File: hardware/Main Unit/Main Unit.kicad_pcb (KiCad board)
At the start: 2 copper layers, 6 parts, among them U1 MCXN547VKLT, U2 TLV71333PDBV

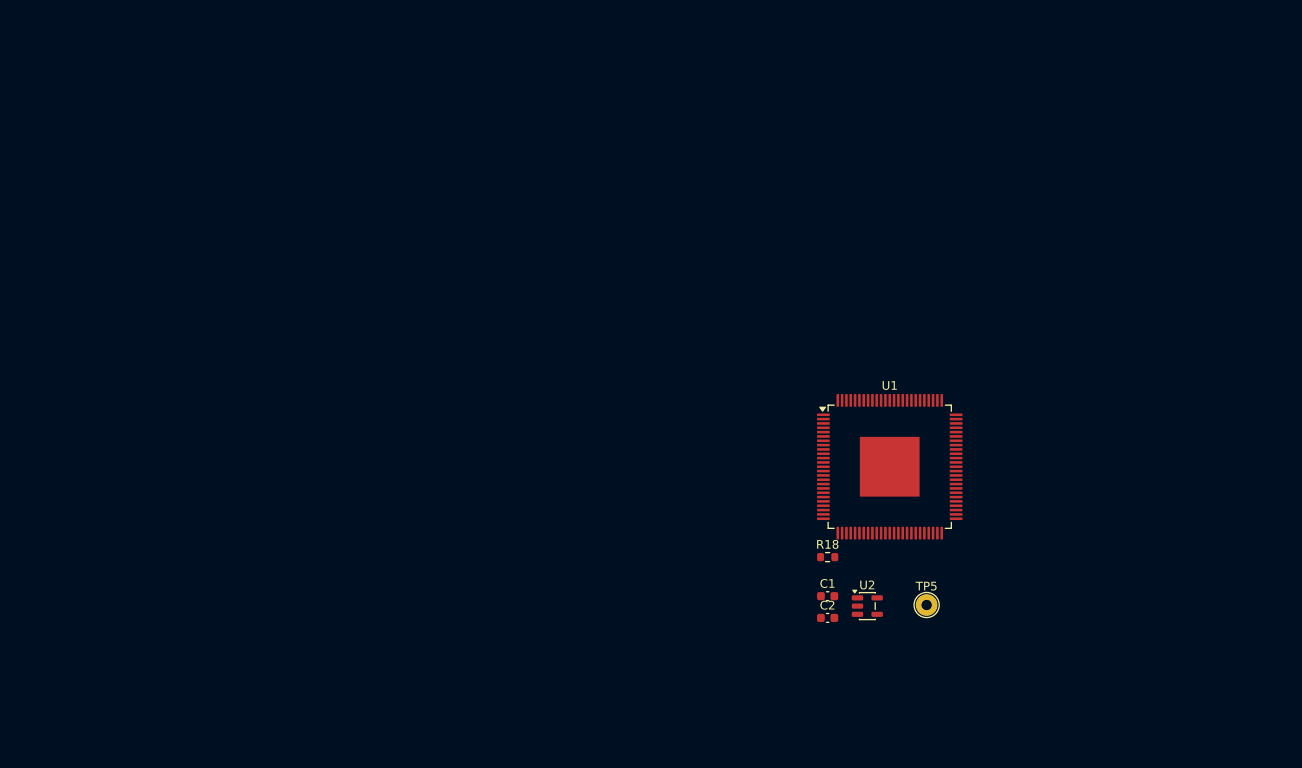
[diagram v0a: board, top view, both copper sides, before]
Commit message: Implement card connector schematic
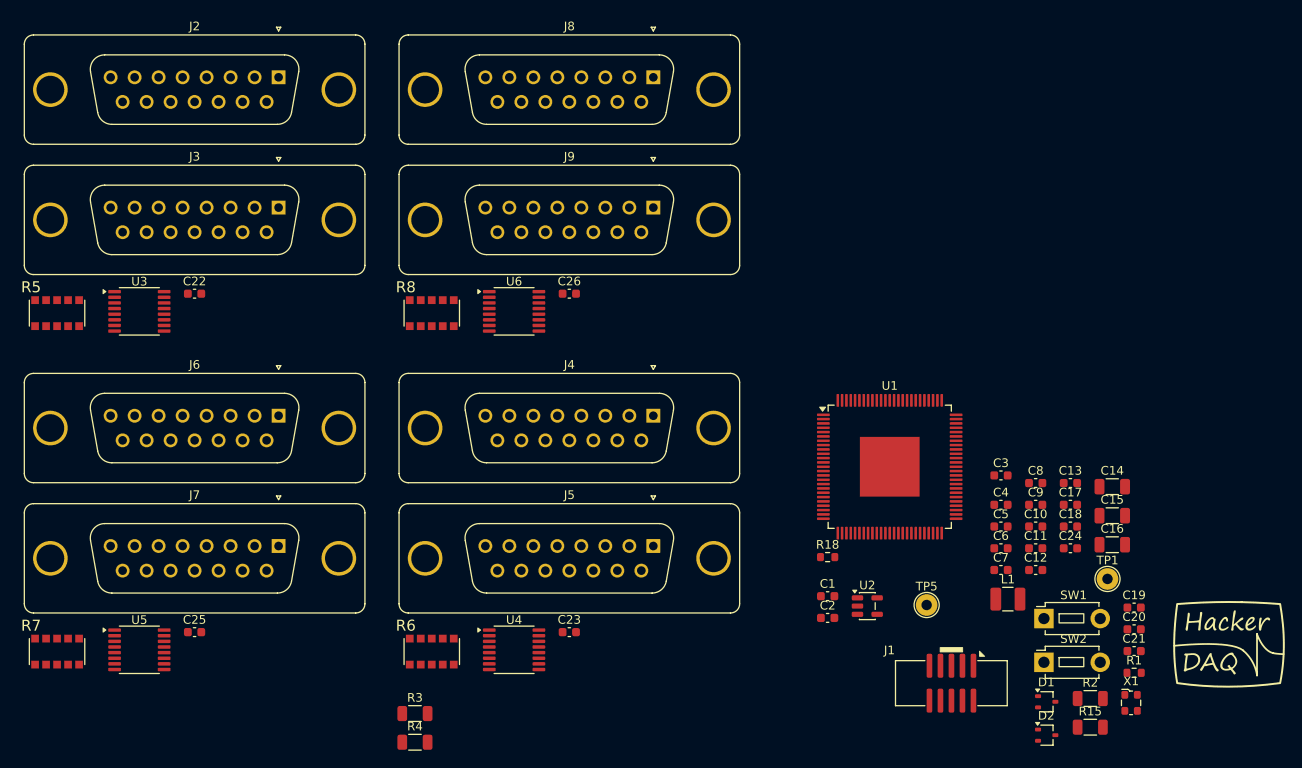
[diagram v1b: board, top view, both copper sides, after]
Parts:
- added C10: 1µF, Capacitor_SMD:C_0603_1608Metric, F.Cu at (177.7, 106.9)
- added C11: 100nF, Capacitor_SMD:C_0603_1608Metric, F.Cu at (177.7, 109.4)
- added C12: 100nF, Capacitor_SMD:C_0603_1608Metric, F.Cu at (177.7, 111.9)
- added C13: 100nF, Capacitor_SMD:C_0603_1608Metric, F.Cu at (181.7, 101.9)
- added C14: 2.2µF, Capacitor_SMD:C_1206_3216Metric, F.Cu at (186.5, 102.3)
- added C15: 10µF, Capacitor_SMD:C_1206_3216Metric, F.Cu at (186.5, 105.7)
- added C16: 10µF, Capacitor_SMD:C_1206_3216Metric, F.Cu at (186.5, 109.0)
- added C17: 100nF, Capacitor_SMD:C_0603_1608Metric, F.Cu at (181.7, 104.4)
- added C18: 220nF, Capacitor_SMD:C_0603_1608Metric, F.Cu at (181.7, 106.9)
- added C19: 100nF, Capacitor_SMD:C_0603_1608Metric, F.Cu at (189.0, 116.3)
- added C20: 100nF, Capacitor_SMD:C_0603_1608Metric, F.Cu at (189.0, 118.8)
- added C21: 100nF, Capacitor_SMD:C_0603_1608Metric, F.Cu at (189.0, 121.3)
- added C22: 100nF, Capacitor_SMD:C_0603_1608Metric, F.Cu at (80.6, 80.0)
- added C23: 100nF, Capacitor_SMD:C_0603_1608Metric, F.Cu at (123.8, 119.1)
- added C24: 1µF, Capacitor_SMD:C_0603_1608Metric, F.Cu at (181.7, 109.4)
- added C25: 100nF, Capacitor_SMD:C_0603_1608Metric, F.Cu at (80.6, 119.1)
- added C26: 100nF, Capacitor_SMD:C_0603_1608Metric, F.Cu at (123.8, 80.0)
- added C3: 100nF, Capacitor_SMD:C_0603_1608Metric, F.Cu at (173.7, 101.0)
- added C4: 100nF, Capacitor_SMD:C_0603_1608Metric, F.Cu at (173.7, 104.4)
- added C5: 100nF, Capacitor_SMD:C_0603_1608Metric, F.Cu at (173.7, 106.9)
- added C6: 100nF, Capacitor_SMD:C_0603_1608Metric, F.Cu at (173.7, 109.4)
- added C7: 1µF, Capacitor_SMD:C_0603_1608Metric, F.Cu at (173.7, 111.9)
- added C8: 100nF, Capacitor_SMD:C_0603_1608Metric, F.Cu at (177.7, 101.9)
- added C9: 100nF, Capacitor_SMD:C_0603_1608Metric, F.Cu at (177.7, 104.4)
- added D1: BAT54W, Package_TO_SOT_SMD:SOT-323_SC-70, F.Cu at (179.0, 127.1)
- added D2: BAT54W, Package_TO_SOT_SMD:SOT-323_SC-70, F.Cu at (179.0, 131.0)
- added J1: 3221-10-0300-00, Project Library:3221-10-0300-00, F.Cu at (170.5, 125.0)
- added J2: 61801525123, Project Library:Wurth_61801525123, F.Cu at (90.3, 55.0)
- added J3: 61801525123, Project Library:Wurth_61801525123, F.Cu at (90.3, 70.1)
- added J4: 61801525123, Project Library:Wurth_61801525123, F.Cu at (133.5, 94.1)
- added J5: 61801525123, Project Library:Wurth_61801525123, F.Cu at (133.5, 109.2)
- added J6: 61801525123, Project Library:Wurth_61801525123, F.Cu at (90.3, 94.1)
- added J7: 61801525123, Project Library:Wurth_61801525123, F.Cu at (90.3, 109.2)
- added J8: 61801525123, Project Library:Wurth_61801525123, F.Cu at (133.5, 55.0)
- added J9: 61801525123, Project Library:Wurth_61801525123, F.Cu at (133.5, 70.1)
- added L1: 1.5µH, Inductor_SMD:L_1210_3225Metric, F.Cu at (174.5, 115.3)
- added LG1: ~, Project Library:HackerDAQ Logo, F.Cu at (199.7, 119.7)
- added R1: 2.2k, Resistor_SMD:R_0603_1608Metric, F.Cu at (189.0, 123.8)
- added R15: 10k, Resistor_SMD:R_1206_3216Metric, F.Cu at (184.0, 130.1)
- added R2: 10k, Resistor_SMD:R_1206_3216Metric, F.Cu at (184.0, 126.8)
- added R3: 10k, Resistor_SMD:R_1206_3216Metric, F.Cu at (106.0, 128.5)
- added R4: 10k, Resistor_SMD:R_1206_3216Metric, F.Cu at (106.0, 131.8)
- added R5: 10k, Project Library:CTS 745C101, F.Cu at (64.7, 82.3)
- added R6: 10k, Project Library:CTS 745C101, F.Cu at (108.0, 121.3)
- added R7: 10k, Project Library:CTS 745C101, F.Cu at (64.7, 121.3)
- added R8: 10k, Project Library:CTS 745C101, F.Cu at (108.0, 82.3)
- added SW1: MJTP1243, Button_Switch_THT:SW_PUSH_1P1T_6x3.5mm_H4.3_APEM_MJTP1243, F.Cu at (178.6, 117.5)
- added SW2: MJTP1243, Button_Switch_THT:SW_PUSH_1P1T_6x3.5mm_H4.3_APEM_MJTP1243, F.Cu at (178.6, 122.6)
- added TP1: VCORE, TestPoint:TestPoint_THTPad_D2.5mm_Drill1.2mm, F.Cu at (186.0, 113.0)
- added U3: SN74CB3Q3257PWR, Package_SO:TSSOP-16_4.4x5mm_P0.65mm, F.Cu at (74.2, 82.1)
- added U4: SN74CB3Q3257PWR, Package_SO:TSSOP-16_4.4x5mm_P0.65mm, F.Cu at (117.5, 121.1)
- added U5: SN74CB3Q3257PWR, Package_SO:TSSOP-16_4.4x5mm_P0.65mm, F.Cu at (74.2, 121.1)
- added U6: SN74CB3Q3257PWR, Package_SO:TSSOP-16_4.4x5mm_P0.65mm, F.Cu at (117.5, 82.1)
- added X1: 24.0000MHz, Oscillator:Oscillator_SMD_ECS_2520MV-xxx-xx-4Pin_2.5x2.0mm, F.Cu at (188.7, 127.3)
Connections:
- U1 pad 1: unconnected-(U1C-P1_8-Pad1) -> /CARD_BUS_0_SPI.MOSI
- U1 pad 10: unconnected-(U1B-EXTAL48M/P1_31-Pad10) -> /MCU/CLK_24MHZ
- U1 pad 101: unconnected-(U1A-VSS-Pad101) -> GND
- U1 pad 12: unconnected-(U1A-VDD_CORE-Pad12) -> /MCU/VCORE
- U1 pad 2: unconnected-(U1C-P1_9-Pad2) -> /CARD_BUS_0_SPI.SCLK
- U1 pad 29: unconnected-(U1A-P4_7/VREFI/VREFO-Pad29) -> Net-(U1A-P4_7/VREFI/VREFO)
- U1 pad 3: unconnected-(U1C-P1_10-Pad3) -> /CARD_BUS_0_SPI.MISO
- U1 pad 31: unconnected-(U1A-VREFH-Pad31) -> +3.3VA
- U1 pad 32: unconnected-(U1A-VREFL-Pad32) -> GND
- U1 pad 33: unconnected-(U1A-VSS_P4-Pad33) -> GND
- U1 pad 4: unconnected-(U1C-P1_11-Pad4) -> /CARD_BUS_0_SPI.~{CS}0
- U1 pad 52: unconnected-(U1A-VSS_DCDC-Pad52) -> GND
- U1 pad 53: unconnected-(U1A-DCDC_LX-Pad53) -> Net-(U1A-DCDC_LX)
- U1 pad 54: unconnected-(U1A-VDD_DCDC/VDD_LDO_SYS-Pad54) -> +3.3V
- U1 pad 55: unconnected-(U1A-VDD_SYS-Pad55) -> /MCU/VDD_SYS
- U1 pad 58: unconnected-(U1A-VDD_CORE-Pad58) -> /MCU/VCORE
- U1 pad 76: unconnected-(U1B-SWDIO/P0_0/TMS-Pad76) -> /MCU/SWDIO
- U1 pad 77: unconnected-(U1B-SWCLK/P0_1/TCLK-Pad77) -> /MCU/SWCLK
- U1 pad 82: unconnected-(U1B-ISPMODE_N/P0_6-Pad82) -> /MCU/~{ISPMODE}
- U1 pad 90: unconnected-(U1C-P0_22-Pad90) -> /CARD_BUS_0_SPI.~{CS}1
- U1 pad 91: unconnected-(U1C-P0_23-Pad91) -> /CARD_BUS_0_SPI.CARD_SEL
- U1 pad 92: unconnected-(U1C-P1_0-Pad92) -> /CARD_BUS_0_SPI.~{CS}2
- U1 pad 93: unconnected-(U1C-P1_1-Pad93) -> /CARD_BUS_0_SPI.~{DRDY}

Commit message: Add MicroSD card, finish MCU symbol
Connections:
- U1 pad 14: (no net) -> unconnected-(U1D-P2_0-Pad14)
- U1 pad 15: (no net) -> unconnected-(U1D-P2_1-Pad15)
- U1 pad 16: (no net) -> unconnected-(U1D-P2_2-Pad16)
- U1 pad 17: (no net) -> unconnected-(U1D-P2_3-Pad17)
- U1 pad 18: (no net) -> unconnected-(U1D-P2_4-Pad18)
- U1 pad 19: (no net) -> unconnected-(U1D-P2_5-Pad19)
- U1 pad 20: (no net) -> unconnected-(U1D-P2_6-Pad20)
- U1 pad 21: (no net) -> unconnected-(U1D-P2_7-Pad21)
- U1 pad 22: (no net) -> unconnected-(U1E-P4_0-Pad22)
- U1 pad 23: (no net) -> unconnected-(U1E-P4_1-Pad23)
- U1 pad 24: (no net) -> unconnected-(U1E-P4_2-Pad24)
- U1 pad 25: (no net) -> unconnected-(U1E-P4_3-Pad25)
- U1 pad 26: (no net) -> unconnected-(U1E-P4_4-Pad26)
- U1 pad 27: (no net) -> unconnected-(U1E-P4_5-Pad27)
- U1 pad 28: (no net) -> unconnected-(U1E-P4_6-Pad28)
- U1 pad 35: (no net) -> unconnected-(U1E-P4_12-Pad35)
- U1 pad 36: (no net) -> unconnected-(U1E-P4_13-Pad36)
- U1 pad 37: (no net) -> unconnected-(U1E-P4_15-Pad37)
- U1 pad 38: (no net) -> unconnected-(U1E-P4_16-Pad38)
- U1 pad 39: (no net) -> unconnected-(U1E-P4_17-Pad39)
- U1 pad 40: (no net) -> unconnected-(U1F-USB1_DP-Pad40)
- U1 pad 41: (no net) -> unconnected-(U1F-USB1_DM-Pad41)
- U1 pad 42: (no net) -> unconnected-(U1F-USB1_VBUS-Pad42)
- U1 pad 45: (no net) -> unconnected-(U1F-USB0_DM-Pad45)
- U1 pad 46: (no net) -> unconnected-(U1F-USB0_DP-Pad46)
- U1 pad 50: (no net) -> unconnected-(U1E-P5_2-Pad50)
- U1 pad 56: (no net) -> unconnected-(U1D-P3_21-Pad56)
- U1 pad 57: (no net) -> unconnected-(U1D-P3_20-Pad57)
- U1 pad 60: (no net) -> unconnected-(U1D-P3_17-Pad60)
- U1 pad 61: (no net) -> unconnected-(U1D-P3_16-Pad61)
- U1 pad 62: (no net) -> unconnected-(U1D-P3_15-Pad62)
- U1 pad 63: (no net) -> unconnected-(U1D-P3_14-Pad63)
- U1 pad 64: (no net) -> unconnected-(U1D-P3_13-Pad64)
- U1 pad 65: (no net) -> unconnected-(U1D-P3_12-Pad65)
- U1 pad 67: (no net) -> unconnected-(U1D-P3_11-Pad67)
- U1 pad 68: (no net) -> unconnected-(U1D-P3_10-Pad68)
- U1 pad 69: (no net) -> unconnected-(U1D-P3_9-Pad69)
- U1 pad 70: (no net) -> unconnected-(U1D-P3_8-Pad70)
- U1 pad 71: (no net) -> unconnected-(U1D-P3_7-Pad71)
- U1 pad 72: (no net) -> unconnected-(U1D-P3_6-Pad72)
- U1 pad 74: (no net) -> unconnected-(U1D-P3_1-Pad74)
- U1 pad 75: (no net) -> unconnected-(U1D-P3_0-Pad75)

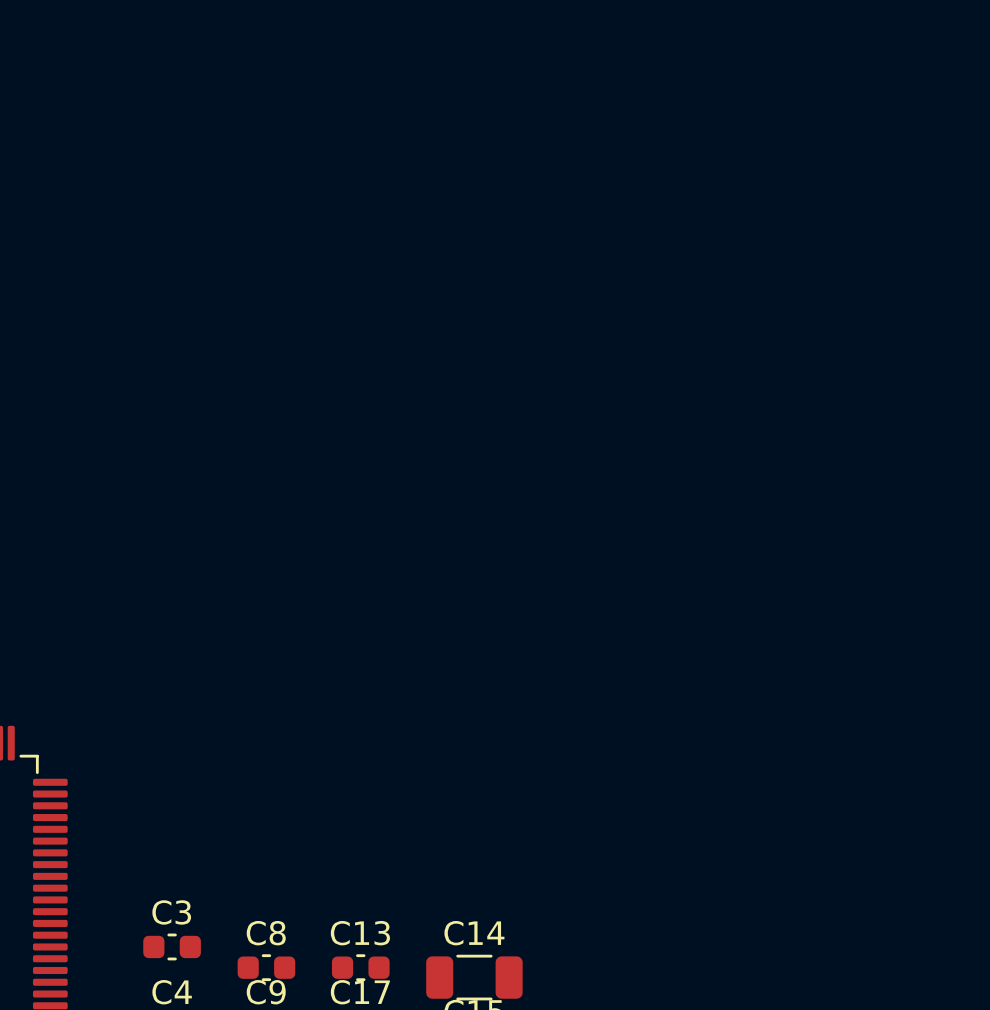
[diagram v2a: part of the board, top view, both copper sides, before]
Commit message: Start on Digital IO card
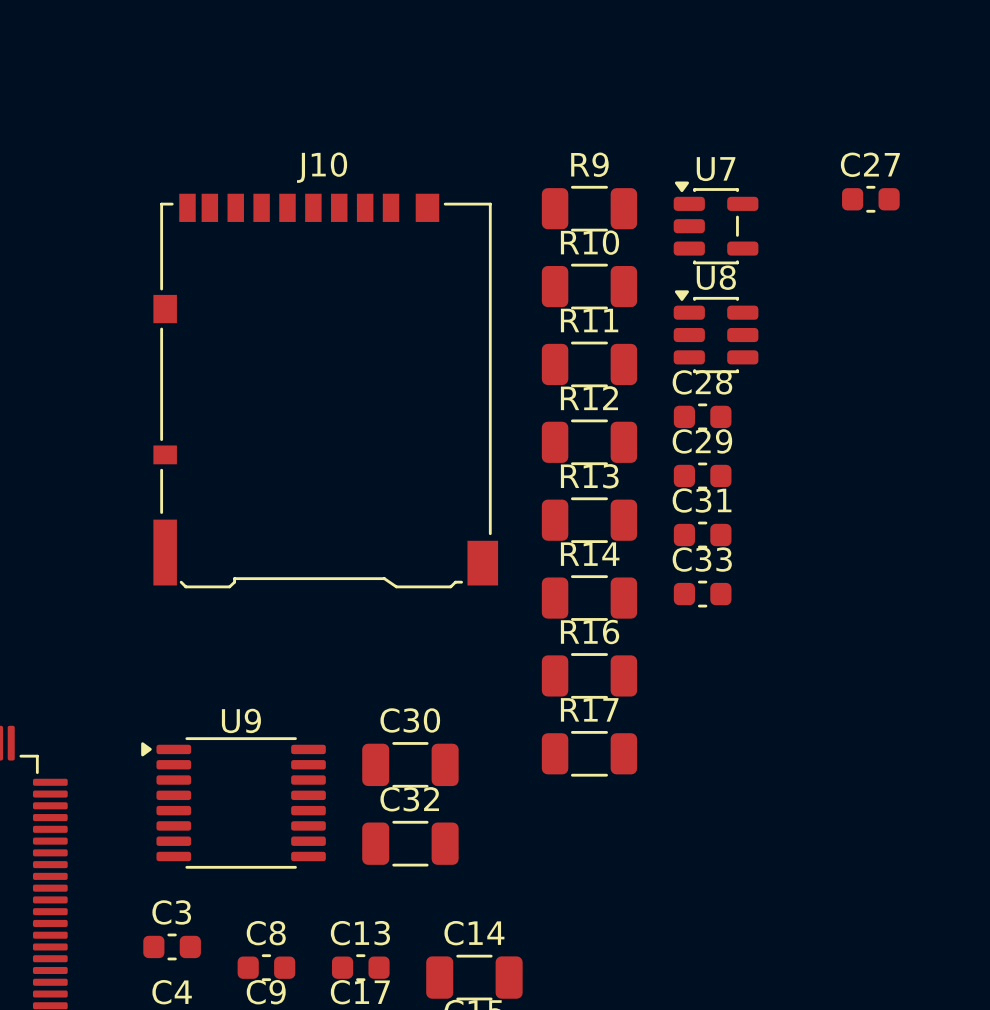
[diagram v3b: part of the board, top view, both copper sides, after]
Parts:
- added C27: 100nF, Capacitor_SMD:C_0603_1608Metric, F.Cu at (203.4, 69.2)
- added C28: 1µF, Capacitor_SMD:C_0603_1608Metric, F.Cu at (196.2, 78.5)
- added C29: 1µF, Capacitor_SMD:C_0603_1608Metric, F.Cu at (196.2, 81.0)
- added C30: 1u, Capacitor_SMD:C_1206_3216Metric, F.Cu at (183.8, 93.3)
- added C31: 1µF, Capacitor_SMD:C_0603_1608Metric, F.Cu at (196.2, 83.5)
- added C32: 10u, Capacitor_SMD:C_1206_3216Metric, F.Cu at (183.8, 96.6)
- added C33: 100nF, Capacitor_SMD:C_0603_1608Metric, F.Cu at (196.2, 86.0)
- added J10: DM3AT, Connector_Card:microSD_HC_Hirose_DM3AT-SF-PEJM5, F.Cu at (180.2, 77.3)
- added R10: 10k, Resistor_SMD:R_1206_3216Metric, F.Cu at (191.4, 72.9)
- added R11: 10k, Resistor_SMD:R_1206_3216Metric, F.Cu at (191.4, 76.2)
- added R12: 10k, Resistor_SMD:R_1206_3216Metric, F.Cu at (191.4, 79.5)
- added R13: 10k, Resistor_SMD:R_1206_3216Metric, F.Cu at (191.4, 82.9)
- added R14: 10k, Resistor_SMD:R_1206_3216Metric, F.Cu at (191.4, 86.2)
- added R16: 10k, Resistor_SMD:R_1206_3216Metric, F.Cu at (191.4, 89.5)
- added R17: 10k, Resistor_SMD:R_1206_3216Metric, F.Cu at (191.4, 92.8)
- added R9: 1k, Resistor_SMD:R_1206_3216Metric, F.Cu at (191.4, 69.6)
- added U7: 74AHC1G04, Package_TO_SOT_SMD:SOT-23-5, F.Cu at (196.8, 70.4)
- added U8: AP22913W6-7, Package_TO_SOT_SMD:SOT-23-6, F.Cu at (196.8, 75.0)
- added U9: SN74AXC4T774, Package_SO:TSSOP-16_4.4x5mm_P0.65mm, F.Cu at (176.6, 94.9)
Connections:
- J4 pad 10: /Card Bus Connectors1/CARD_SPI.~{DRDY} -> /CARD_BUS_1_SPI.~{DRDY}
- J4 pad 12: /Card Bus Connectors1/CARD_SPI.MISO -> /CARD_BUS_1_SPI.MISO
- J4 pad 13: /Card Bus Connectors1/CARD_SPI.MOSI -> /CARD_BUS_1_SPI.MOSI
- J4 pad 14: /Card Bus Connectors1/CARD_SPI.SCLK -> /CARD_BUS_1_SPI.SCLK
- J5 pad 10: /Card Bus Connectors1/CARD_SPI.~{DRDY} -> /CARD_BUS_1_SPI.~{DRDY}
- J5 pad 12: /Card Bus Connectors1/CARD_SPI.MISO -> /CARD_BUS_1_SPI.MISO
- J5 pad 13: /Card Bus Connectors1/CARD_SPI.MOSI -> /CARD_BUS_1_SPI.MOSI
- J5 pad 14: /Card Bus Connectors1/CARD_SPI.SCLK -> /CARD_BUS_1_SPI.SCLK
- J6 pad 10: /Card Bus Connectors2/CARD_SPI.~{DRDY} -> /CARD_BUS_2_SPI.~{DRDY}
- J6 pad 12: /Card Bus Connectors2/CARD_SPI.MISO -> /CARD_BUS_2_SPI.MISO
- J6 pad 13: /Card Bus Connectors2/CARD_SPI.MOSI -> /CARD_BUS_2_SPI.MOSI
- J6 pad 14: /Card Bus Connectors2/CARD_SPI.SCLK -> /CARD_BUS_2_SPI.SCLK
- J7 pad 10: /Card Bus Connectors2/CARD_SPI.~{DRDY} -> /CARD_BUS_2_SPI.~{DRDY}
- J7 pad 12: /Card Bus Connectors2/CARD_SPI.MISO -> /CARD_BUS_2_SPI.MISO
- J7 pad 13: /Card Bus Connectors2/CARD_SPI.MOSI -> /CARD_BUS_2_SPI.MOSI
- J7 pad 14: /Card Bus Connectors2/CARD_SPI.SCLK -> /CARD_BUS_2_SPI.SCLK
- J8 pad 10: /Card Bus Connectors3/CARD_SPI.~{DRDY} -> /CARD_BUS_3_SPI.~{DRDY}
- J8 pad 12: /Card Bus Connectors3/CARD_SPI.MISO -> /CARD_BUS_3_SPI.MISO
- J8 pad 13: /Card Bus Connectors3/CARD_SPI.MOSI -> /CARD_BUS_3_SPI.MOSI
- J8 pad 14: /Card Bus Connectors3/CARD_SPI.SCLK -> /CARD_BUS_3_SPI.SCLK
- J9 pad 10: /Card Bus Connectors3/CARD_SPI.~{DRDY} -> /CARD_BUS_3_SPI.~{DRDY}
- J9 pad 12: /Card Bus Connectors3/CARD_SPI.MISO -> /CARD_BUS_3_SPI.MISO
- J9 pad 13: /Card Bus Connectors3/CARD_SPI.MOSI -> /CARD_BUS_3_SPI.MOSI
- J9 pad 14: /Card Bus Connectors3/CARD_SPI.SCLK -> /CARD_BUS_3_SPI.SCLK
- U1 pad 14: unconnected-(U1D-P2_0-Pad14) -> /CARD_BUS_3_SPI.~{CS}1
- U1 pad 15: unconnected-(U1D-P2_1-Pad15) -> /CARD_BUS_3_SPI.CARD_SEL
- U1 pad 16: unconnected-(U1D-P2_2-Pad16) -> /CARD_BUS_3_SPI.~{CS}0
- U1 pad 17: unconnected-(U1D-P2_3-Pad17) -> /CARD_BUS_3_SPI.SCLK
- U1 pad 18: unconnected-(U1D-P2_4-Pad18) -> /CARD_BUS_3_SPI.MOSI
- U1 pad 19: unconnected-(U1D-P2_5-Pad19) -> /CARD_BUS_3_SPI.MISO
- U1 pad 20: unconnected-(U1D-P2_6-Pad20) -> /CARD_BUS_3_SPI.~{DRDY}
- U1 pad 21: unconnected-(U1D-P2_7-Pad21) -> /CARD_BUS_3_SPI.~{CS}2
- U1 pad 43: (no net) -> GND
- U1 pad 50: unconnected-(U1E-P5_2-Pad50) -> /CARD_BUS_1_SPI.CARD_SEL
- U1 pad 51: (no net) -> /CARD_BUS_1_SPI.~{DRDY}
- U1 pad 56: unconnected-(U1D-P3_21-Pad56) -> /CARD_BUS_2_SPI.~{CS}2
- U1 pad 57: unconnected-(U1D-P3_20-Pad57) -> /CARD_BUS_2_SPI.~{CS}1
- U1 pad 60: unconnected-(U1D-P3_17-Pad60) -> /CARD_BUS_2_SPI.~{CS}0
- U1 pad 61: unconnected-(U1D-P3_16-Pad61) -> /CARD_BUS_2_SPI.MISO
- U1 pad 62: unconnected-(U1D-P3_15-Pad62) -> /CARD_BUS_2_SPI.SCLK
- U1 pad 63: unconnected-(U1D-P3_14-Pad63) -> /CARD_BUS_2_SPI.MOSI
- U1 pad 64: unconnected-(U1D-P3_13-Pad64) -> /CARD_BUS_2_SPI.CARD_SEL
- U1 pad 65: unconnected-(U1D-P3_12-Pad65) -> /CARD_BUS_1_SPI.~{CS}0
- U1 pad 67: unconnected-(U1D-P3_11-Pad67) -> /MCU/uSD_SPI_FC6.~{CS}
- U1 pad 68: unconnected-(U1D-P3_10-Pad68) -> /MCU/uSD_SPI_FC6.MISO
- U1 pad 69: unconnected-(U1D-P3_9-Pad69) -> /CARD_BUS_1_SPI.MISO
- U1 pad 70: unconnected-(U1D-P3_8-Pad70) -> /CARD_BUS_1_SPI.MOSI
- U1 pad 71: unconnected-(U1D-P3_7-Pad71) -> /CARD_BUS_1_SPI.SCLK
- U1 pad 72: unconnected-(U1D-P3_6-Pad72) -> /MCU/uSD_SPI_FC6.SCLK
- U1 pad 73: (no net) -> +3.3V
- U1 pad 74: unconnected-(U1D-P3_1-Pad74) -> /MCU/uSD_SPI_FC6.MOSI
- U1 pad 75: unconnected-(U1D-P3_0-Pad75) -> /CARD_BUS_2_SPI.~{DRDY}
- U1 pad 78: unconnected-(U1C-P0_2-Pad78) -> /CARD_BUS_1_SPI.~{CS}1
- U1 pad 79: unconnected-(U1C-P0_3-Pad79) -> /CARD_BUS_1_SPI.~{CS}2
- U1 pad 9: (no net) -> Net-(U1B-RESET_B)
- U4 pad 1: /Card Bus Connectors1/CARD_SPI.CARD_SEL -> /CARD_BUS_1_SPI.CARD_SEL
- U4 pad 4: /Card Bus Connectors1/CARD_SPI.~{CS}0 -> /CARD_BUS_1_SPI.~{CS}0
- U4 pad 7: /Card Bus Connectors1/CARD_SPI.~{CS}1 -> /CARD_BUS_1_SPI.~{CS}1
- U4 pad 9: /Card Bus Connectors1/CARD_SPI.~{CS}2 -> /CARD_BUS_1_SPI.~{CS}2
- U5 pad 1: /Card Bus Connectors2/CARD_SPI.CARD_SEL -> /CARD_BUS_2_SPI.CARD_SEL
- U5 pad 4: /Card Bus Connectors2/CARD_SPI.~{CS}0 -> /CARD_BUS_2_SPI.~{CS}0
- U5 pad 7: /Card Bus Connectors2/CARD_SPI.~{CS}1 -> /CARD_BUS_2_SPI.~{CS}1
- U5 pad 9: /Card Bus Connectors2/CARD_SPI.~{CS}2 -> /CARD_BUS_2_SPI.~{CS}2
- U6 pad 1: /Card Bus Connectors3/CARD_SPI.CARD_SEL -> /CARD_BUS_3_SPI.CARD_SEL
- U6 pad 4: /Card Bus Connectors3/CARD_SPI.~{CS}0 -> /CARD_BUS_3_SPI.~{CS}0
- U6 pad 7: /Card Bus Connectors3/CARD_SPI.~{CS}1 -> /CARD_BUS_3_SPI.~{CS}1
- U6 pad 9: /Card Bus Connectors3/CARD_SPI.~{CS}2 -> /CARD_BUS_3_SPI.~{CS}2
